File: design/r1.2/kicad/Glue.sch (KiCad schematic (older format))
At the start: 28 parts, among them IC2 ATF16V8BQL-15PU, IC5 ATF16V8BQL, IC6 74174N, IC8 555N, IC9 74LS01N, Q2 5H8ET-10.000, Q3 5H8ET-4.000

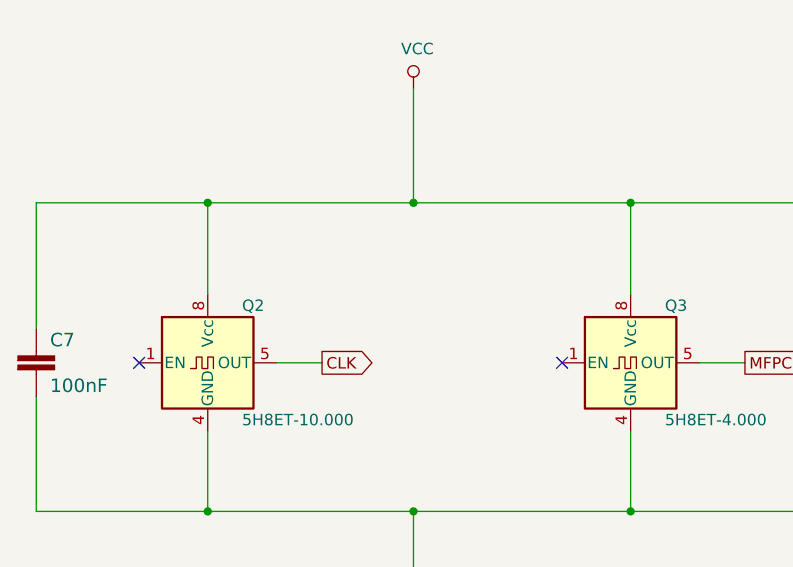
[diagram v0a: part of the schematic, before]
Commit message: Pull-up on oscillator enables
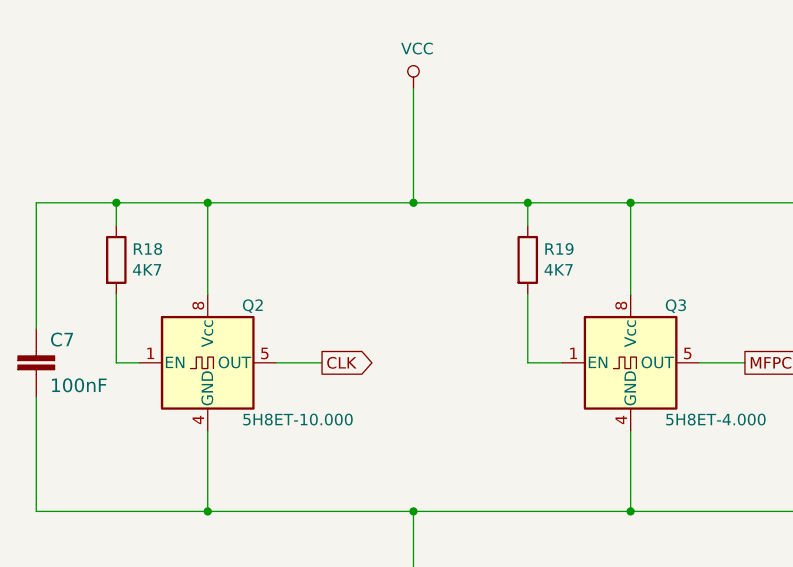
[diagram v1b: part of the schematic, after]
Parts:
- added R18, R19: 4K7, symbol Device:R
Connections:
- net VCC: now also R18.1, R19.1
- net at Q2.1 (EN): now also R18.2
- net at Q3.1 (EN): now also R19.2
- no-connect marks 10 -> 8
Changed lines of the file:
@@
 Text GLabel 4450 3750 2    50   Output ~ 0
 CLK
-NoConn ~ 5500 3750
-NoConn ~ 3650 3750
 Wire Wire Line
 	3950 3050 4850 3050
@@
 Connection ~ 4850 3050
 Wire Wire Line
-	4850 3050 5800 3050
+	4850 3050 5350 3050
 Wire Wire Line
 	4850 4700 4850 4400
@@
 	3200 3600 3200 3050
 Wire Wire Line
-	3200 3050 3950 3050
+	3200 3050 3550 3050
 Connection ~ 3950 3050
 Wire Wire Line
@@
 Wire Wire Line
 	8600 3800 8600 4600
+$Comp
+L Device:R R18
+U 1 1 5ECFB250
+P 3550 3300
+F 0 "R18" H 3620 3346 50  0000 L CNN
+F 1 "4K7" H 3620 3255 50  0000 L CNN
+F 2 "" V 3480 3300 50  0001 C CNN
+F 3 "~" H 3550 3300 50  0001 C CNN
+	1    3550 3300
+	1    0    0    -1
+$EndComp
+$Comp
+L Device:R R19
+U 1 1 5ECFC0DF
+P 5350 3300
+F 0 "R19" H 5420 3346 50  0000 L CNN
+F 1 "4K7" H 5420 3255 50  0000 L CNN
+F 2 "" V 5280 3300 50  0001 C CNN
+F 3 "~" H 5350 3300 50  0001 C CNN
+	1    5350 3300
+	1    0    0    -1
+$EndComp
+Wire Wire Line
+	5350 3450 5350 3750
+Wire Wire Line
+	5350 3750 5500 3750
+Wire Wire Line
+	5350 3150 5350 3050
+Connection ~ 5350 3050
+Wire Wire Line
+	5350 3050 5800 3050
+Wire Wire Line
+	3550 3150 3550 3050
+Connection ~ 3550 3050
+Wire Wire Line
+	3550 3050 3950 3050
+Wire Wire Line
+	3550 3450 3550 3750
+Wire Wire Line
+	3550 3750 3650 3750
 Wire Bus Line
 	12850 2600 12850 3800

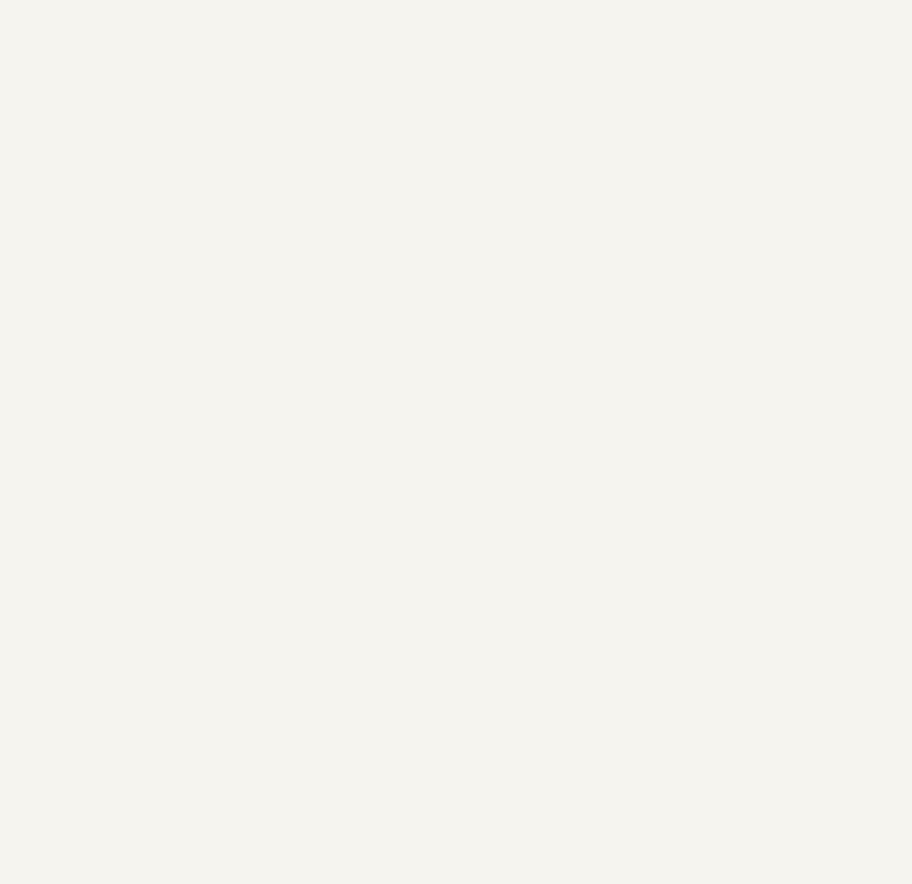
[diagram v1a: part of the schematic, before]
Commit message: More robust MFP decoding
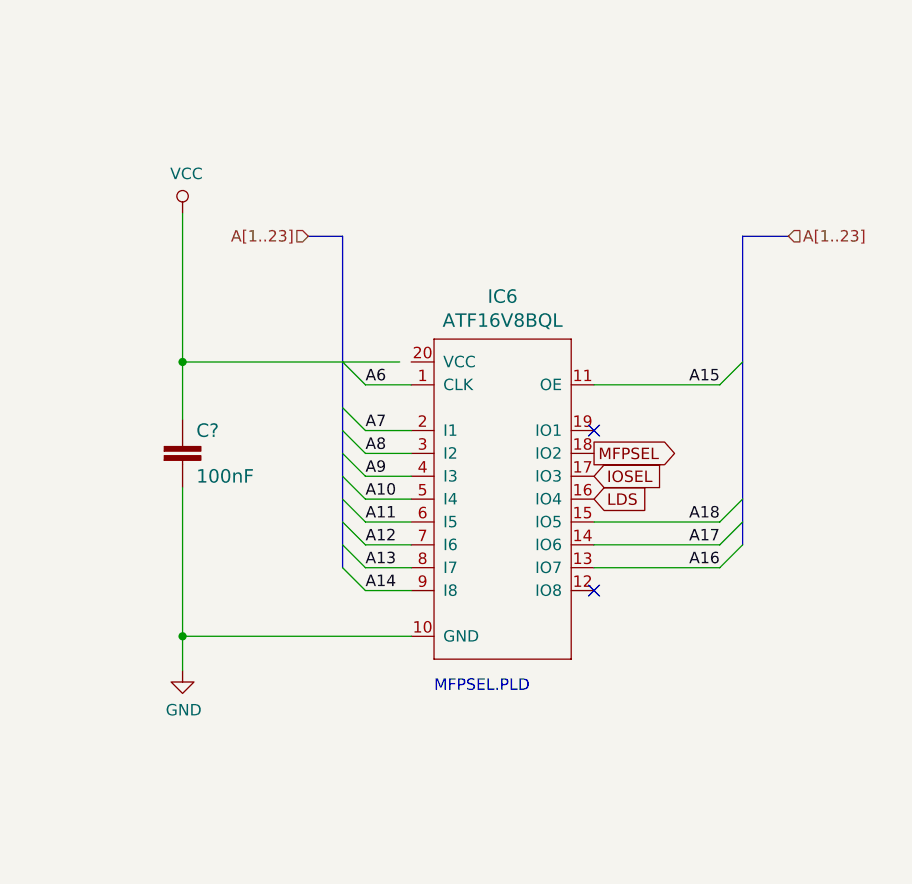
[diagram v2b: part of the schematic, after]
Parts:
- added C?: 100nF, rosco_m68k:C2.5-3, symbol rosco_m68k-eagle-import:C2,5-3
- added IC6: ATF16V8BQL, rosco_m68k:DIL20, symbol rosco_m68k-eagle-import:ATF16V8BP3
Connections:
- net A18: now also IC6.15 (IO5)
- net GND: now also C?.2, IC6.10 (GND)
- net IOSEL: now also IC6.17 (IO3)
- net LDS: now also IC6.16 (IO4)
- net VCC: now also C?.1
- new net A10: IC6.5 (I4)
- new net A11: IC6.6 (I5)
- new net A12: IC6.7 (I6)
- new net A13: IC6.8 (I7)
- new net A14: IC6.9 (I8)
- new net A15: IC6.11 (OE)
- new net A16: IC6.13 (IO7)
- new net A17: IC6.14 (IO6)
- new net A6: IC6.1 (CLK)
- new net A7: IC6.2 (I1)
- new net A8: IC6.3 (I2)
- new net A9: IC6.4 (I3)
- new net MFPSEL: IC6.18 (IO2)
- no-connect marks 8 -> 10
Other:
- note added: "MFPSEL.PLD"
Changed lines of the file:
@@
 Wire Wire Line
 	3550 3750 3650 3750
+$Comp
+L rosco_m68k-eagle-import:ATF16V8BP3 IC?
+U 1 1 5EF2F381
+P 20100 7200
+AR Path="/5E53B810/5EF2F381" Ref="IC?"  Part="1"
+AR Path="/5E53B952/5EF2F381" Ref="IC6"  Part="1"
+F 0 "IC6" H 20100 8086 59  0000 C CNN
+F 1 "ATF16V8BQL" H 20100 7981 59  0000 C CNN
+F 2 "rosco_m68k:DIL20" H 20100 7200 50  0001 C CNN
+F 3 "" H 20100 7200 50  0001 C CNN
+	1    20100 7200
+	1    0    0    -1
+$EndComp
+Text Notes 19800 8050 0    50   ~ 0
+MFPSEL.PLD
+Text GLabel 20500 7200 2    50   Input ~ 0
+LDS
+Text GLabel 20500 7100 2    50   Input ~ 0
+IOSEL
+Text GLabel 20500 7000 2    50   Output ~ 0
+MFPSEL
+NoConn ~ 20500 6900
+NoConn ~ 20500 7600
+Wire Bus Line
+	19400 6050 19250 6050
+Text HLabel 19250 6050 0    50   Input ~ 0
+A[1..23]
+Entry Wire Line
+	19400 6600 19500 6700
+Entry Wire Line
+	19400 6800 19500 6900
+Entry Wire Line
+	19400 6900 19500 7000
+Entry Wire Line
+	19400 7000 19500 7100
+Entry Wire Line
+	19400 7100 19500 7200
+Entry Wire Line
+	19400 7200 19500 7300
+Entry Wire Line
+	19400 7300 19500 7400
+Entry Wire Line
+	19400 7400 19500 7500
+Entry Wire Line
+	19400 7500 19500 7600
+Wire Bus Line
+	21150 6050 21350 6050
+Text HLabel 21350 6050 2    50   Input ~ 0
+A[1..23]
+Entry Wire Line
+	21050 7500 21150 7400
+Wire Wire Line
+	20500 7500 21050 7500
+Wire Wire Line
+	20500 7300 21050 7300
+Wire Wire Line
+	20500 7400 21050 7400
+Entry Wire Line
+	21050 7300 21150 7200
+Entry Wire Line
+	21050 7400 21150 7300
+Text Label 19500 6700 0    50   ~ 0
+A6
+Text Label 19500 6900 0    50   ~ 0
+A7
+Text Label 19500 7000 0    50   ~ 0
+A8
+Text Label 19500 7100 0    50   ~ 0
+A9
+Text Label 19500 7200 0    50   ~ 0
+A10
+Text Label 19500 7300 0    50   ~ 0
+A11
+Text Label 19500 7400 0    50   ~ 0
+A12
+Text Label 19500 7500 0    50   ~ 0
+A13
+Text Label 19500 7600 0    50   ~ 0
+A14
+Entry Wire Line
+	21050 6700 21150 6600
+Wire Wire Line
+	21050 6700 20500 6700
+Text Label 21050 6700 2    50   ~ 0
+A15
+Text Label 21050 7500 2    50   ~ 0
+A16
+Text Label 21050 7400 2    50   ~ 0
+A17
+Text Label 21050 7300 2    50   ~ 0
+A18
+$Comp
+L power:VCC #PWR?
+U 1 1 5F056E21
+P 18700 5950
+F 0 "#PWR?" H 18700 5800 50  0001 C CNN
+F 1 "VCC" H 18717 6123 50  0000 C CNN
+F 2 "" H 18700 5950 50  0001 C CNN
+F 3 "" H 18700 5950 50  0001 C CNN
+	1    18700 5950
+	1    0    0    -1
+$EndComp
+$Comp
+L power:GND #PWR?
+U 1 1 5F057711
+P 18700 7950
+F 0 "#PWR?" H 18700 7700 50  0001 C CNN
+F 1 "GND" H 18705 7777 50  0000 C CNN
+F 2 "" H 18700 7950 50  0001 C CNN
+F 3 "" H 18700 7950 50  0001 C CNN
+	1    18700 7950
+	1    0    0    -1
+$EndComp
+$Comp
+L rosco_m68k-eagle-import:C2,5-3 C?
+U 1 1 5F060B7D
+P 18700 6950
+AR Path="/5F060B7D" Ref="C?"  Part="1"
+AR Path="/5E53B630/5F060B7D" Ref="C?"  Part="1"
+AR Path="/5E53B952/5F060B7D" Ref="C?"  Part="1"
+F 0 "C?" H 18760 6965 59  0000 L BNN
+F 1 "100nF" H 18760 6765 59  0000 L BNN
+F 2 "rosco_m68k:C2.5-3" H 18700 6950 50  0001 C CNN
+F 3 "" H 18700 6950 50  0001 C CNN
+	1    18700 6950
+	1    0    0    -1
+$EndComp
+Wire Wire Line
+	19500 6700 19700 6700
+Wire Wire Line
+	19500 6900 19700 6900
+Wire Wire Line
+	19500 7000 19700 7000
+Wire Wire Line
+	19500 7100 19700 7100
+Wire Wire Line
+	19500 7200 19700 7200
+Wire Wire Line
+	19500 7300 19700 7300
+Wire Wire Line
+	19500 7400 19700 7400
+Wire Wire Line
+	19500 7500 19700 7500
+Wire Wire Line
+	19500 7600 19700 7600
+Wire Wire Line
+	18700 5950 18700 6600
+Connection ~ 18700 6600
+Wire Wire Line
+	18700 6600 18700 6850
+Wire Wire Line
+	19700 7800 18700 7800
+Wire Wire Line
+	18700 7150 18700 7800
+Wire Wire Line
+	18700 6600 19650 6600
+Wire Bus Line
+	21150 6050 21150 7400
 Wire Bus Line
 	12850 2600 12850 3800
+Wire Bus Line
+	19400 6050 19400 7500
+Connection ~ 18700 7800
+Wire Wire Line
+	18700 7800 18700 7950
 $EndSCHEMATC

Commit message: Layout for 1.2 and PLD changes for same
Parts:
- R3: renamed from R18; footprint (none) -> rosco_m68k:0207_10
- R8: renamed from R19; footprint (none) -> rosco_m68k:0207_10
- gave numbers to parts that had none: 1
- renumbered IC6 to IC3
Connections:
- net A17: now also IC5.11 (OE)
- net EVENROMSEL: now also IC5.5 (I4); no longer IC5.6 (I5)
- net GND: no longer C25.-, IC5.11 (OE)
- net ODDRAMSEL: now also IC5.6 (I5); no longer IC5.5 (I4)
- net VCC: now also IC3.20 (VCC)
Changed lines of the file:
@@
 Wire Wire Line
 	9450 8000 9450 8300
-Text GLabel 9450 8000 0    10   BiDi ~ 0
-GND
 Wire Wire Line
 	11250 7700 11350 7700
@@
 P 9450 6400
 AR Path="/F401FE7E" Ref="R12"  Part="1"
-AR Path="/5E53B952/F401FE7E" Ref="R9"  Part="1"
-F 0 "R9" V 9591 6450 59  0000 L BNN
+AR Path="/5E53B952/F401FE7E" Ref="R11"  Part="1"
+F 0 "R11" V 9591 6450 59  0000 L BNN
 F 1 "2K2" V 9480 6450 59  0000 L BNN
 F 2 "rosco_m68k:0207_10" H 9450 6400 50  0001 C CNN
@@
 P 11150 8900
 AR Path="/BDE9F7DA" Ref="R13"  Part="1"
-AR Path="/5E53B952/BDE9F7DA" Ref="R10"  Part="1"
-F 0 "R10" H 11100 8750 59  0000 L BNN
+AR Path="/5E53B952/BDE9F7DA" Ref="R12"  Part="1"
+F 0 "R12" H 11100 8750 59  0000 L BNN
 F 1 "270R" H 11050 9000 59  0000 L BNN
 F 2 "rosco_m68k:0207_10" H 11150 8900 50  0001 C CNN
@@
 P 14750 6500
 AR Path="/59846CAA" Ref="R14"  Part="1"
-AR Path="/5E53B952/59846CAA" Ref="R12"  Part="1"
-F 0 "R12" V 14891 6550 59  0000 L BNN
+AR Path="/5E53B952/59846CAA" Ref="R14"  Part="1"
+F 0 "R14" V 14891 6550 59  0000 L BNN
 F 1 "330R" V 14780 6550 59  0000 L BNN
 F 2 "rosco_m68k:0207_10" H 14750 6500 50  0001 C CNN
@@
 P 15200 6500
 AR Path="/1CDB656C" Ref="R16"  Part="1"
-AR Path="/5E53B952/1CDB656C" Ref="R13"  Part="1"
-F 0 "R13" V 15341 6550 59  0000 L BNN
+AR Path="/5E53B952/1CDB656C" Ref="R15"  Part="1"
+F 0 "R15" V 15341 6550 59  0000 L BNN
 F 1 "4K7" V 15230 6550 59  0000 L BNN
 F 2 "rosco_m68k:0207_10" H 15200 6500 50  0001 C CNN
@@
 P 15850 6500
 AR Path="/120757BD" Ref="R17"  Part="1"
-AR Path="/5E53B952/120757BD" Ref="R14"  Part="1"
-F 0 "R14" V 15991 6550 59  0000 L BNN
+AR Path="/5E53B952/120757BD" Ref="R16"  Part="1"
+F 0 "R16" V 15991 6550 59  0000 L BNN
 F 1 "4K7" V 15880 6550 59  0000 L BNN
 F 2 "rosco_m68k:0207_10" H 15850 6500 50  0001 C CNN
@@
 P 14150 6500
 AR Path="/FD2CBBBB" Ref="R15"  Part="1"
-AR Path="/5E53B952/FD2CBBBB" Ref="R11"  Part="1"
-F 0 "R11" V 14291 6550 59  0000 L BNN
+AR Path="/5E53B952/FD2CBBBB" Ref="R13"  Part="1"
+F 0 "R13" V 14291 6550 59  0000 L BNN
 F 1 "1K2" V 14180 6550 59  0000 L BNN
 F 2 "rosco_m68k:0207_10" H 14150 6500 50  0001 C CNN
@@
 P 3750 7500
 AR Path="/51A2EE5C" Ref="R4"  Part="1"
-AR Path="/5E53B952/51A2EE5C" Ref="R3"  Part="1"
-F 0 "R3" V 3600 7559 59  0000 L BNN
+AR Path="/5E53B952/51A2EE5C" Ref="R4"  Part="1"
+F 0 "R4" V 3600 7559 59  0000 L BNN
 F 1 "4K7" V 3780 7550 59  0000 L BNN
 F 2 "rosco_m68k:0207_10" H 3750 7500 50  0001 C CNN
@@
 P 4150 7500
 AR Path="/5F990599" Ref="R6"  Part="1"
-AR Path="/5E53B952/5F990599" Ref="R4"  Part="1"
-F 0 "R4" V 4000 7559 59  0000 L BNN
+AR Path="/5E53B952/5F990599" Ref="R5"  Part="1"
+F 0 "R5" V 4000 7559 59  0000 L BNN
 F 1 "4K7" V 4180 7550 59  0000 L BNN
 F 2 "rosco_m68k:0207_10" H 4150 7500 50  0001 C CNN
@@
 P 4550 7500
 AR Path="/A57FCB1C" Ref="R7"  Part="1"
-AR Path="/5E53B952/A57FCB1C" Ref="R5"  Part="1"
-F 0 "R5" V 4400 7559 59  0000 L BNN
+AR Path="/5E53B952/A57FCB1C" Ref="R6"  Part="1"
+F 0 "R6" V 4400 7559 59  0000 L BNN
 F 1 "4K7" V 4580 7550 59  0000 L BNN
 F 2 "rosco_m68k:0207_10" H 4550 7500 50  0001 C CNN
@@
 P 4950 7500
 AR Path="/88AE9C44" Ref="R8"  Part="1"
-AR Path="/5E53B952/88AE9C44" Ref="R6"  Part="1"
-F 0 "R6" V 4800 7559 59  0000 L BNN
+AR Path="/5E53B952/88AE9C44" Ref="R7"  Part="1"
+F 0 "R7" V 4800 7559 59  0000 L BNN
 F 1 "4K7" V 4980 7550 59  0000 L BNN
 F 2 "rosco_m68k:0207_10" H 4950 7500 50  0001 C CNN
@@
 P 5350 7500
 AR Path="/949C8759" Ref="R9"  Part="1"
-AR Path="/5E53B952/949C8759" Ref="R7"  Part="1"
-F 0 "R7" V 5200 7559 59  0000 L BNN
+AR Path="/5E53B952/949C8759" Ref="R9"  Part="1"
+F 0 "R9" V 5200 7559 59  0000 L BNN
 F 1 "4K7" V 5380 7550 59  0000 L BNN
 F 2 "rosco_m68k:0207_10" H 5350 7500 50  0001 C CNN
@@
 P 5750 7500
 AR Path="/755AD31A" Ref="R11"  Part="1"
-AR Path="/5E53B952/755AD31A" Ref="R8"  Part="1"
-F 0 "R8" V 5600 7559 59  0000 L BNN
+AR Path="/5E53B952/755AD31A" Ref="R10"  Part="1"
+F 0 "R10" V 5600 7559 59  0000 L BNN
 F 1 "4K7" V 5780 7550 59  0000 L BNN
 F 2 "rosco_m68k:0207_10" H 5750 7500 50  0001 C CNN
@@
 ODDROMSEL
 Text GLabel 9500 3500 0    47   Input ~ 0
+EVENROMSEL
+Text GLabel 9500 3600 0    47   Input ~ 0
 ODDRAMSEL
-Text GLabel 9500 3600 0    47   Input ~ 0
-EVENROMSEL
 Text GLabel 9500 3700 0    47   Input ~ 0
 EVENRAMSEL
@@
 $EndComp
 NoConn ~ 10300 3900
-NoConn ~ 10300 3200
 $Comp
 L power:GND #PWR?
@@
 Wire Wire Line
 	9450 5900 9450 6200
-Text GLabel 14850 3600 2    47   Output ~ 0
+Text GLabel 14850 3600 2    47   Input ~ 0
 IACK
 Text GLabel 14850 3800 2    47   Output ~ 0
@@
 Connection ~ 13400 4400
 Wire Wire Line
-	11000 3000 11000 4600
-Wire Wire Line
-	10300 3000 11000 3000
-Wire Wire Line
-	9100 4600 11000 4600
-Wire Wire Line
 	8600 2900 8600 3500
 Wire Wire Line
 	8600 3800 8600 4600
 $Comp
-L Device:R R18
+L Device:R R3
 U 1 1 5ECFB250
 P 3550 3300
-F 0 "R18" H 3620 3346 50  0000 L CNN
+F 0 "R3" H 3620 3346 50  0000 L CNN
 F 1 "4K7" H 3620 3255 50  0000 L CNN
-F 2 "" V 3480 3300 50  0001 C CNN
+F 2 "rosco_m68k:0207_10" V 3480 3300 50  0001 C CNN
 F 3 "~" H 3550 3300 50  0001 C CNN
 	1    3550 3300
@@
 $EndComp
 $Comp
-L Device:R R19
+L Device:R R8
 U 1 1 5ECFC0DF
 P 5350 3300
-F 0 "R19" H 5420 3346 50  0000 L CNN
+F 0 "R8" H 5420 3346 50  0000 L CNN
 F 1 "4K7" H 5420 3255 50  0000 L CNN
-F 2 "" V 5280 3300 50  0001 C CNN
+F 2 "rosco_m68k:0207_10" V 5280 3300 50  0001 C CNN
 F 3 "~" H 5350 3300 50  0001 C CNN
 	1    5350 3300
@@
 P 20100 7200
 AR Path="/5E53B810/5EF2F381" Ref="IC?"  Part="1"
-AR Path="/5E53B952/5EF2F381" Ref="IC6"  Part="1"
-F 0 "IC6" H 20100 8086 59  0000 C CNN
+AR Path="/5E53B952/5EF2F381" Ref="IC3"  Part="1"
+F 0 "IC3" H 20100 8086 59  0000 C CNN
 F 1 "ATF16V8BQL" H 20100 7981 59  0000 C CNN
 F 2 "rosco_m68k:DIL20" H 20100 7200 50  0001 C CNN
@@
 A18
 $Comp
-L power:VCC #PWR?
+L power:VCC #PWR0110
 U 1 1 5F056E21
 P 18700 5950
-F 0 "#PWR?" H 18700 5800 50  0001 C CNN
+F 0 "#PWR0110" H 18700 5800 50  0001 C CNN
 F 1 "VCC" H 18717 6123 50  0000 C CNN
 F 2 "" H 18700 5950 50  0001 C CNN
@@
 $EndComp
 $Comp
-L power:GND #PWR?
+L power:GND #PWR0111
 U 1 1 5F057711
 P 18700 7950
-F 0 "#PWR?" H 18700 7700 50  0001 C CNN
+F 0 "#PWR0111" H 18700 7700 50  0001 C CNN
 F 1 "GND" H 18705 7777 50  0000 C CNN
 F 2 "" H 18700 7950 50  0001 C CNN
@@
 AR Path="/5F060B7D" Ref="C?"  Part="1"
 AR Path="/5E53B630/5F060B7D" Ref="C?"  Part="1"
-AR Path="/5E53B952/5F060B7D" Ref="C?"  Part="1"
-F 0 "C?" H 18760 6965 59  0000 L BNN
+AR Path="/5E53B952/5F060B7D" Ref="C13"  Part="1"
+F 0 "C13" H 18760 6965 59  0000 L BNN
 F 1 "100nF" H 18760 6765 59  0000 L BNN
 F 2 "rosco_m68k:C2.5-3" H 18700 6950 50  0001 C CNN
@@
 Wire Wire Line
 	18700 7150 18700 7800
-Wire Wire Line
-	18700 6600 19650 6600
+Connection ~ 18700 7800
+Wire Wire Line
+	18700 7800 18700 7950
+NoConn ~ 10300 3200
+Text GLabel 10300 3000 2    50   Input ~ 0
+A17
+Wire Wire Line
+	18700 6600 19700 6600
 Wire Bus Line
 	21150 6050 21150 7400
@@
 Wire Bus Line
 	19400 6050 19400 7500
-Connection ~ 18700 7800
-Wire Wire Line
-	18700 7800 18700 7950
 $EndSCHEMATC
